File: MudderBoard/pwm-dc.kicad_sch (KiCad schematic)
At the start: 0 parts

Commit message: Added PWM-DC Circuit
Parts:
- added C18, C58: 4.7uF, symbol Device:C
- added C59, C60, C61: 10uF, symbol Device:C
- added R42, R43: 500, symbol Device:R_US
- added R44: 1.58k, symbol Device:R_US
- added R45: 1.15k, symbol Device:R_US
- added R46, R47, R48: 4.7k, symbol Device:R_US
- added U6, U8: UA741, symbol Amplifier_Operational:LM741
- added U7: LM339, symbol Comparator:LM339
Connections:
- new net: U7.10 (-), U8.2 (-), U8.6
- new net: C58.1, R43.2, U8.3 (+)
- new net: U6.2 (-), U6.6, U7.4 (-), U7.6 (-)
- new net: C18.1, R42.2, U6.3 (+)
- new net 5V: R44.2
- new net COMP_VREF: R44.1, R45.2, U7.11 (+), U7.5 (+), U7.7 (+)
- new net GND: C18.2, C58.2, C59.2, C60.2, C61.2, R45.1, U6.1 (NULL), U6.4 (V-), U6.5 (NULL), U7.12 (V-), U8.1 (NULL), U8.4 (V-), U8.5 (NULL)
- new net PWM_CH5: R42.1
- new net PWM_CH6: R43.1
- new net RELAY_1: C59.1, R46.1, U7.2
- new net RELAY_2: C60.1, R47.1, U7.1
- new net RELAY_3: C61.1, R48.1, U7.13
- no-connect marks 0 -> 3
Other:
- note added: "FIGURE OUT WHAT VOLTAGE WE WILL BE POWERING RELAYS WITH"

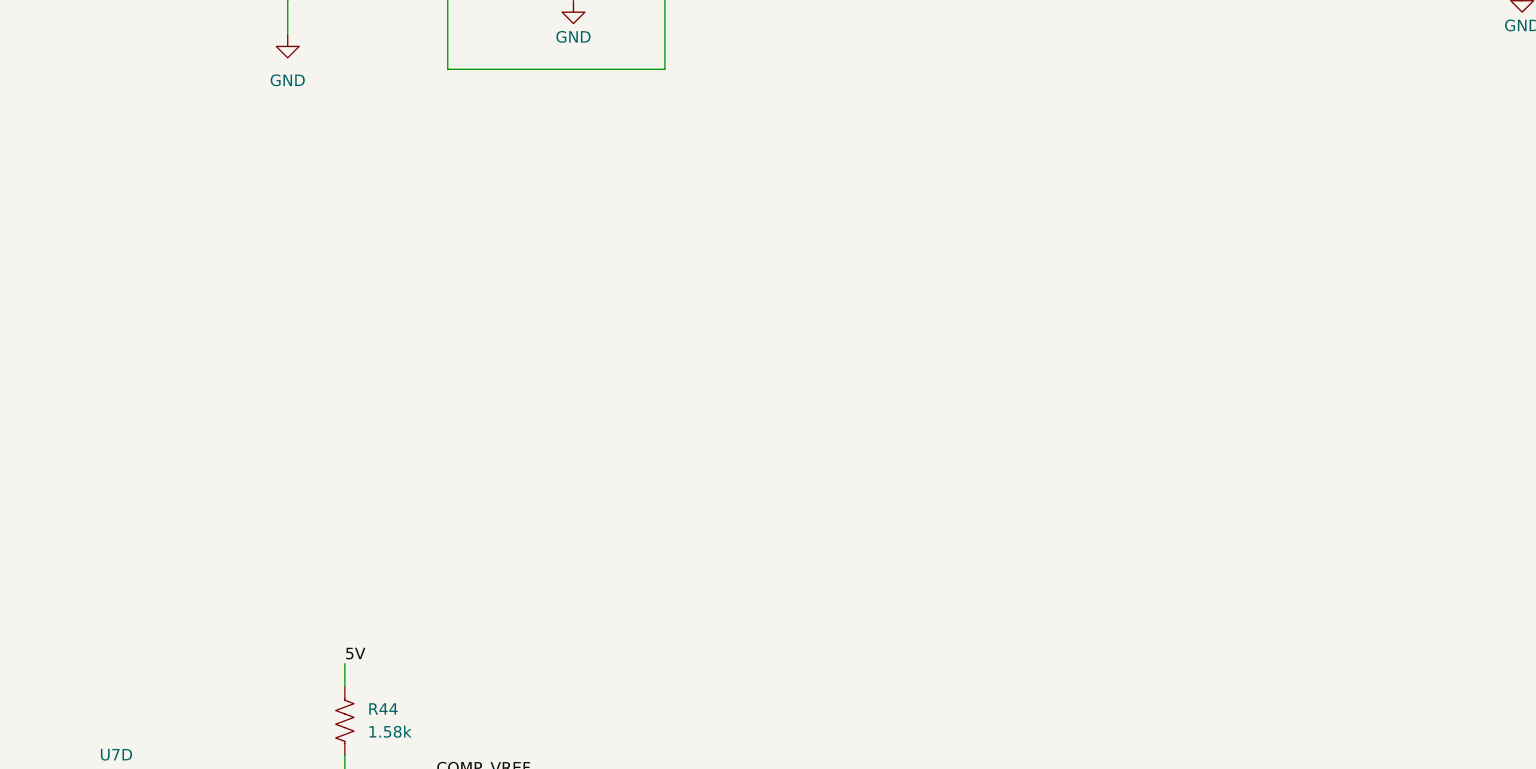
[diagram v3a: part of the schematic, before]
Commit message: added relay driver
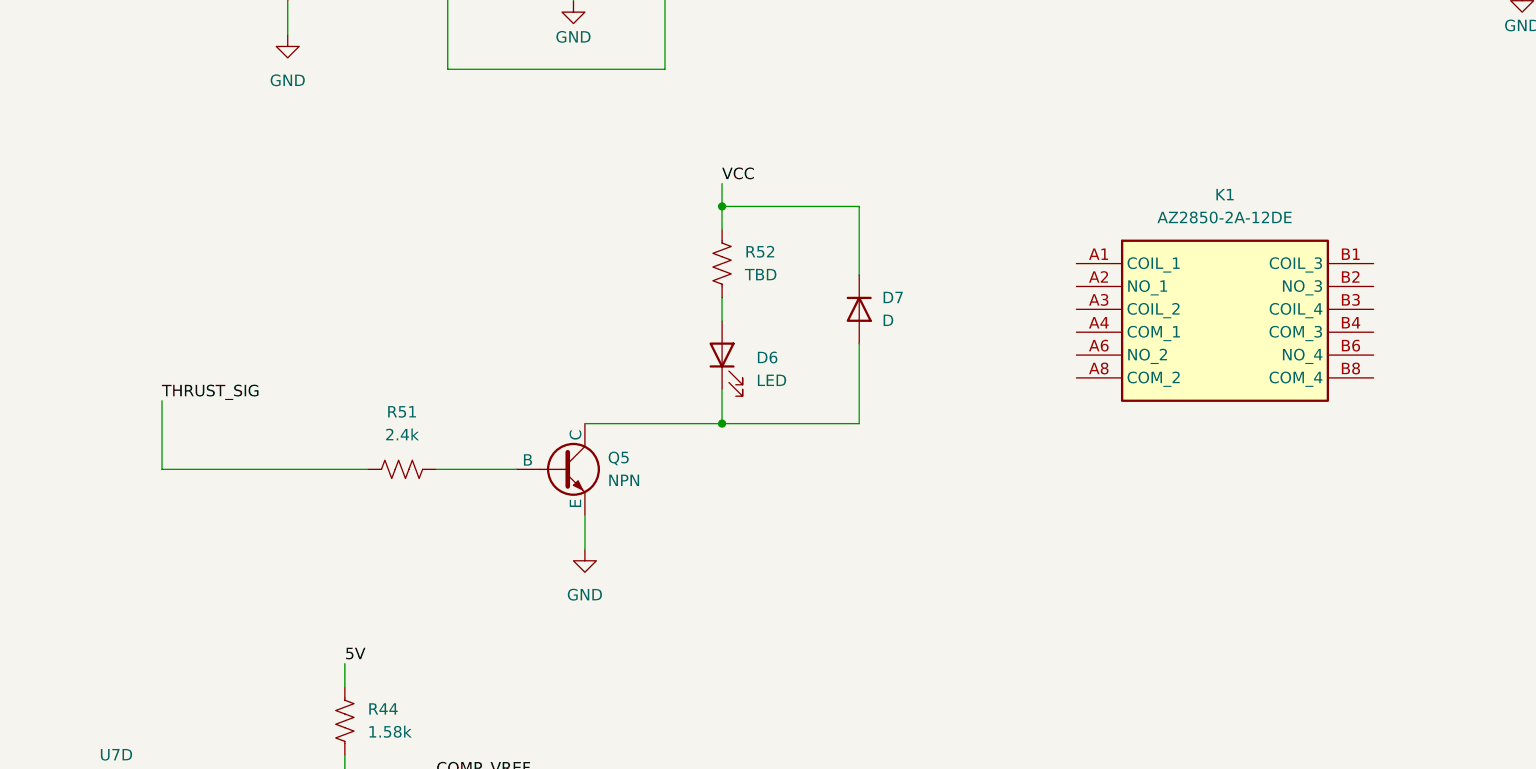
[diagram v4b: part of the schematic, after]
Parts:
- added D6: LED, symbol Device:LED
- added D7: D, symbol Device:D
- added K1: AZ2850-2A-12DE, AZ28502A12DE, symbol AZ2850-2A-12DE:AZ2850-2A-12DE
- added Q5: NPN, symbol Simulation_SPICE:NPN
- added R51: 2.4k, symbol Device:R_US
- added R52: TBD, symbol Device:R_US
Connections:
- net GND: now also Q5.3 (E)
- new net: D6.2 (A), R52.1
- new net: D6.1 (K), D7.2 (A), Q5.1 (C)
- new net: Q5.2 (B), R51.2
- new net THRUST_SIG: R51.1
- new net VCC: D7.1 (K), R52.2

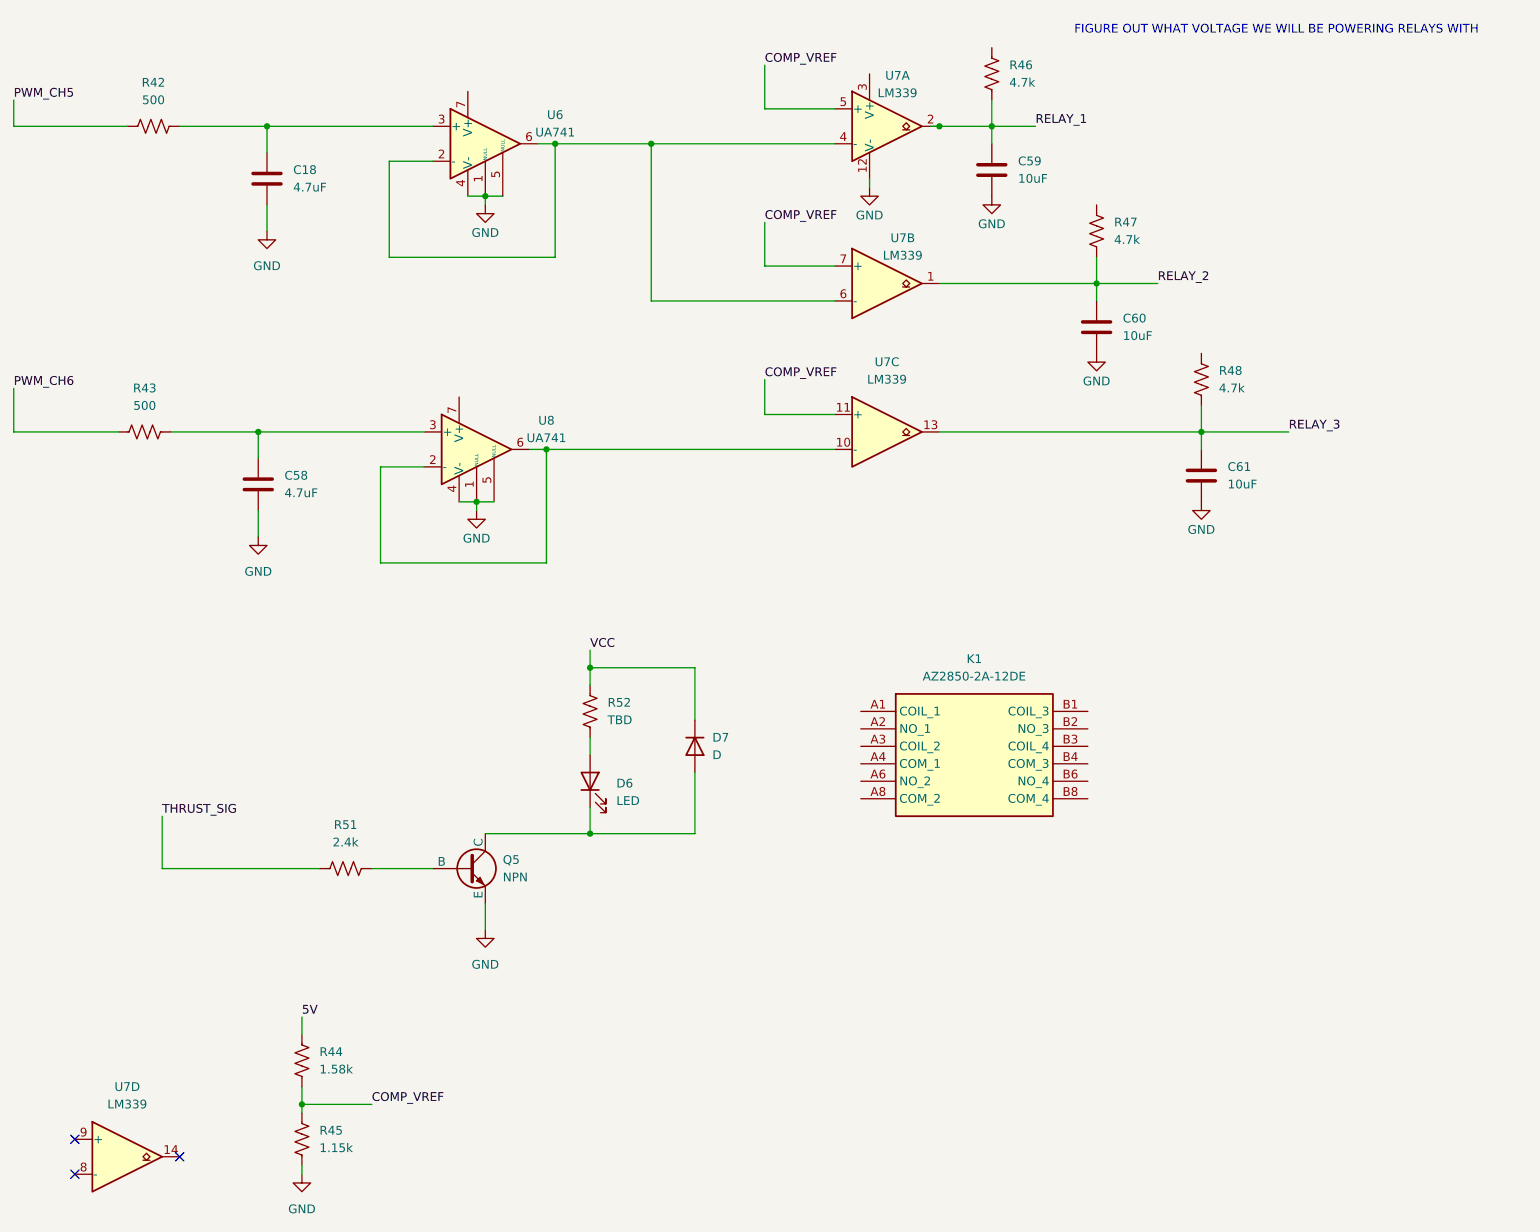
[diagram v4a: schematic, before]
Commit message: connected relay
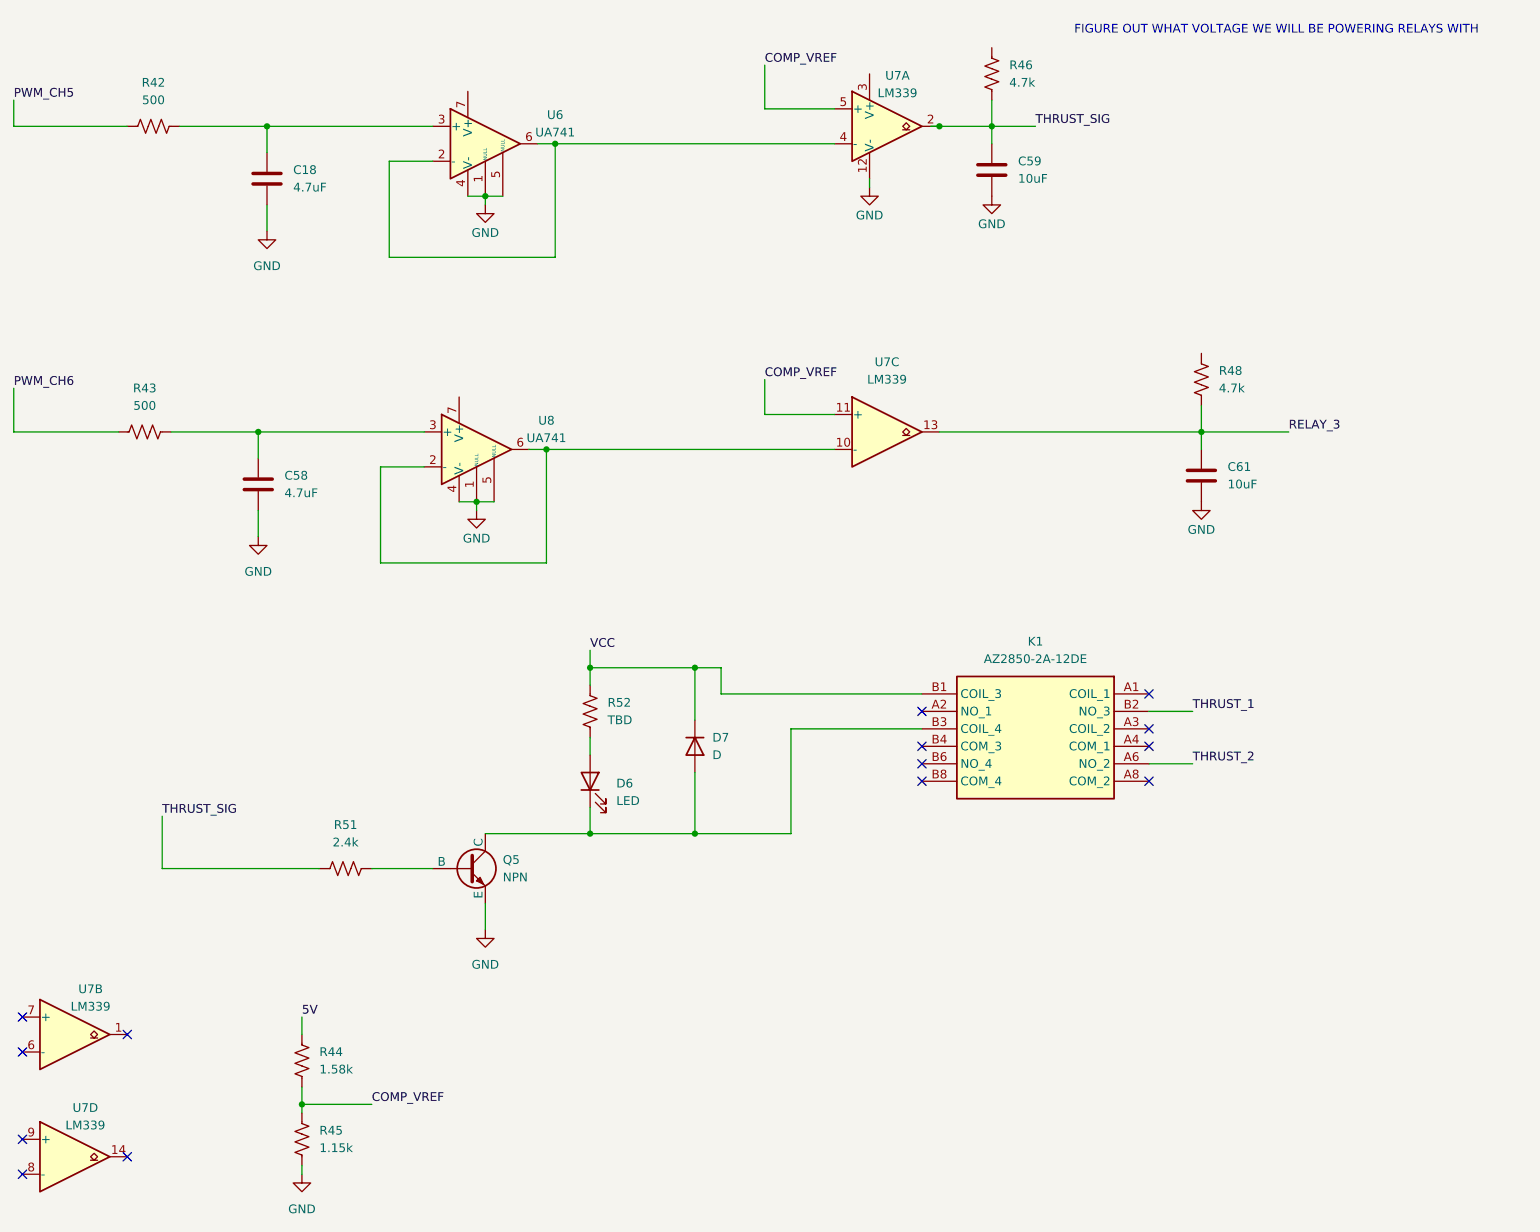
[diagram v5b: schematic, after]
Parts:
- removed C60: 10uF, symbol Device:C
- removed R47: 4.7k, symbol Device:R_US
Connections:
- net RELAY_1 is gone; now on net THRUST_SIG: C59.1, R46.1, U7.2
- net COMP_VREF: no longer U7.7 (+)
- net VCC: now also K1.B1 (COIL_3)
- net at D6.1 (K), D7.2 (A), Q5.1 (C): now also K1.B3 (COIL_4)
- net at U6.2 (-), U6.6, U7.4 (-): no longer U7.6 (-)
- net THRUST_2: now reaches K1.A6 (NO_2)
- net THRUST_1: now reaches K1.B2 (NO_3)
- net RELAY_2: no longer names the net of U7.1
- no-connect marks 3 -> 14
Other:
- moved on the sheet: K1, U7B, U7D

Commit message: added jetson circuit
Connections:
- net VCC is gone; now on net +BATT: D7.1 (K), K1.B1 (COIL_3), R52.2
- net +BATT: now reaches U8.7 (V+)
- net +BATT: now also R46.2, R48.2, U6.7 (V+)
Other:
- note removed: "FIGURE OUT WHAT VOLTAGE WE WILL BE POWERING RELAYS WITH"
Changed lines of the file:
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@@
+	(wire
+		(pts
+			(xy 195.58 60.96) (xy 195.58 63.5)
+		)
+		(stroke
+			(width 0)
+			(type default)
+		)
+	)
 	(wire
 		(pts
@@
 	(wire
 		(pts
+			(xy 88.9 22.86) (xy 88.9 25.4)
+		)
+		(stroke
+			(width 0)
+			(type default)
+		)
+	)
+	(wire
+		(pts
 			(xy 87.63 85.09) (xy 90.17 85.09)
 		)
@@
 	(wire
 		(pts
+			(xy 87.63 67.31) (xy 87.63 69.85)
+		)
+		(stroke
+			(width 0)
+			(type default)
+		)
+	)
+	(wire
+		(pts
 			(xy 147.32 38.1) (xy 147.32 39.37)
 		)
@@
 	(wire
 		(pts
+			(xy 165.1 16.51) (xy 165.1 19.05)
+		)
+		(stroke
+			(width 0)
+			(type default)
+		)
+	)
+	(wire
+		(pts
 			(xy 64.77 170.18) (xy 64.77 172.72)
 		)
@@
 		)
 	)
-	(text "FIGURE OUT WHAT VOLTAGE WE WILL BE POWERING RELAYS WITH"
-		(exclude_from_sim no)
-		(at 206.502 16.51 0)
-		(effects
-			(font
-				(size 1.27 1.27)
-			)
-		)
-	)
-	(label "VCC"
+	(label "+BATT"
+		(at 88.9 22.86 0)
+		(fields_autoplaced yes)
+		(effects
+			(font
+				(size 1.27 1.27)
+			)
+			(justify left bottom)
+		)
+	)
+	(label "+BATT"
 		(at 106.68 106.68 0)
 		(fields_autoplaced yes)
@@
 		)
 	)
+	(label "+BATT"
+		(at 195.58 60.96 0)
+		(fields_autoplaced yes)
+		(effects
+			(font
+				(size 1.27 1.27)
+			)
+			(justify left bottom)
+		)
+	)
 	(label "THRUST_2"
 		(at 194.31 123.19 0)
@@
 		)
 	)
+	(label "+BATT"
+		(at 87.63 67.31 0)
+		(fields_autoplaced yes)
+		(effects
+			(font
+				(size 1.27 1.27)
+			)
+			(justify left bottom)
+		)
+	)
 	(label "COMP_VREF"
 		(at 132.08 67.31 0)
@@
 		(fields_autoplaced yes)
 		(effects
+			(font
+				(size 1.27 1.27)
+			)
+			(justify left bottom)
+		)
+	)
+	(label "+BATT"
+		(at 165.1 16.51 0)
+		(fields_autoplaced yes)
+		(effects
